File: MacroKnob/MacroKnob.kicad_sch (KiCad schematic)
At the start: 6 parts, among them SW1 RotaryEncoder_Switch_MP, U2 Sparkfun_Pro_Micro

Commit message: update schematic & pcb
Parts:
- added R4, R5, R6, R7: 10K, Resistor_THT:R_Axial_DIN0204_L3.6mm_D1.6mm_P5.08mm_Horizontal, symbol Device:R
- added SW2: Up, Button_Switch_SMD:SW_SPST_CK_RS282G05A3, symbol Switch:SW_Push
- added SW3: Down, Button_Switch_SMD:SW_SPST_CK_RS282G05A3, symbol Switch:SW_Push
- added SW4: H, Button_Switch_SMD:SW_SPST_CK_RS282G05A3, symbol Switch:SW_Push
- added SW5: *, Button_Switch_SMD:SW_SPST_CK_RS282G05A3, symbol Switch:SW_Push
- R1, R2, R3: value R -> 10K
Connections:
- net VCC 5V: now reaches R2.1
- net VCC 5V: now also R3.2
- net DT: now reaches R2.2, SW1.B
- net CLK: now reaches R3.1
- net CLK: now also SW1.A
- net GND: now reaches SW1.C, SW1.S2
- net GND: now also SW2.2, SW3.2, SW4.2, SW5.2
- net SW: now reaches R1.1
- new net: R6.1, SW4.1
- new net: R4.1, SW2.1
- new net: R5.1, SW3.1
- new net: R7.1, SW5.1
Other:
- moved on the sheet: R1, R2, R3, SW1

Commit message: update
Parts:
- added J1: Conn_01x04_Socket, Connector_Samtec:Samtec_FMC_ASP-134486-01_10x40_P1.27mm_Vertical, symbol Connector:Conn_01x04_Socket
- added R8, R9: 10K, Resistor_THT:R_Axial_DIN0204_L3.6mm_D1.6mm_P5.08mm_Horizontal, symbol Device:R
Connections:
- net GND: now also Brd1.1 (GND), J1.4 (Pin_4)
- net VCC: now reaches Brd1.2 (VCC)
- net VCC: now also J1.3 (Pin_3), R8.1, R9.1
- net at Brd1.3 (SCL): now also U2.3 (GND), J1.2 (Pin_2), R9.2
- net at Brd1.4 (SDA): now also U2.2 (D0/RX), J1.1 (Pin_1), R8.2
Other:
- moved on the sheet: Brd1

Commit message: Update Schematic
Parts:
- J1: value Conn_01x04_Socket -> I2C
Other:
- moved on the sheet: R8, R9
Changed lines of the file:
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@@
+	)
+	(junction
+		(at 63.5 86.36)
+		(diameter 0)
+		(color 0 0 0 0)
 	)
 	(junction
@@
 	)
 	(junction
-		(at 64.77 86.36)
-		(diameter 0)
-		(color 0 0 0 0)
-	)
-	(junction
 		(at 50.8 83.82)
 		(diameter 0)
@@
 	(wire
 		(pts
-			(xy 64.77 86.36) (xy 64.77 83.82)
+			(xy 63.5 86.36) (xy 63.5 83.82)
 		)
 		(stroke
@@
 	(wire
 		(pts
-			(xy 53.34 88.9) (xy 57.15 88.9)
+			(xy 53.34 88.9) (xy 55.88 88.9)
 		)
 		(stroke
@@
 	(wire
 		(pts
-			(xy 68.58 86.36) (xy 64.77 86.36)
-		)
-		(stroke
-			(width 0)
-			(type default)
-		)
-	)
-	(wire
-		(pts
 			(xy 143.51 76.2) (xy 143.51 87.63)
 		)
@@
 	(wire
 		(pts
-			(xy 64.77 86.36) (xy 64.77 88.9)
+			(xy 63.5 86.36) (xy 63.5 88.9)
 		)
 		(stroke
@@
 	(wire
 		(pts
+			(xy 63.5 86.36) (xy 68.58 86.36)
+		)
+		(stroke
+			(width 0)
+			(type default)
+		)
+	)
+	(wire
+		(pts
 			(xy 63.5 69.85) (xy 63.5 63.5)
 		)
@@
 	(wire
 		(pts
-			(xy 50.8 83.82) (xy 57.15 83.82)
+			(xy 50.8 83.82) (xy 55.88 83.82)
 		)
 		(stroke
@@
 	(symbol
 		(lib_id "Device:R")
-		(at 60.96 88.9 270)
+		(at 59.69 88.9 270)
 		(unit 1)
 		(exclude_from_sim no)
@@
 		(dnp no)
 		(property "Reference" "R9"
-			(at 60.96 88.9 90)
+			(at 59.69 88.9 90)
 			(effects
 				(font
@@
 		)
 		(property "Value" "10K"
-			(at 60.96 91.186 90)
+			(at 59.69 91.186 90)
 			(effects
 				(font
@@
 		)
 		(property "Footprint" "Resistor_THT:R_Axial_DIN0204_L3.6mm_D1.6mm_P5.08mm_Horizontal"
-			(at 60.96 87.122 90)
+			(at 59.69 87.122 90)
 			(effects
 				(font
@@
 		)
 		(property "Datasheet" "~"
-			(at 60.96 88.9 0)
+			(at 59.69 88.9 0)
 			(effects
 				(font
@@
 		)
 		(property "Description" "Resistor"
-			(at 60.96 88.9 0)
+			(at 59.69 88.9 0)
 			(effects
 				(font
@@
 			)
 		)
-		(property "Value" "Conn_01x04_Socket"
+		(property "Value" "I2C"
 			(at 92.71 74.9299 0)
 			(effects
@@
 	(symbol
 		(lib_id "Device:R")
-		(at 60.96 83.82 270)
+		(at 59.69 83.82 270)
 		(unit 1)
 		(exclude_from_sim no)
@@
 		(dnp no)
 		(property "Reference" "R8"
-			(at 60.96 83.82 90)
+			(at 59.69 83.82 90)
 			(effects
 				(font
@@
 		)
 		(property "Value" "10K"
-			(at 60.96 86.106 90)
+			(at 59.69 86.106 90)
 			(effects
 				(font
@@
 		)
 		(property "Footprint" "Resistor_THT:R_Axial_DIN0204_L3.6mm_D1.6mm_P5.08mm_Horizontal"
-			(at 60.96 82.042 90)
+			(at 59.69 82.042 90)
 			(effects
 				(font
@@
 		)
 		(property "Datasheet" "~"
-			(at 60.96 83.82 0)
+			(at 59.69 83.82 0)
 			(effects
 				(font
@@
 		)
 		(property "Description" "Resistor"
-			(at 60.96 83.82 0)
-			(effects
-				(font
+			(at 59.69 83.82 0)
+			(effects
+				(font

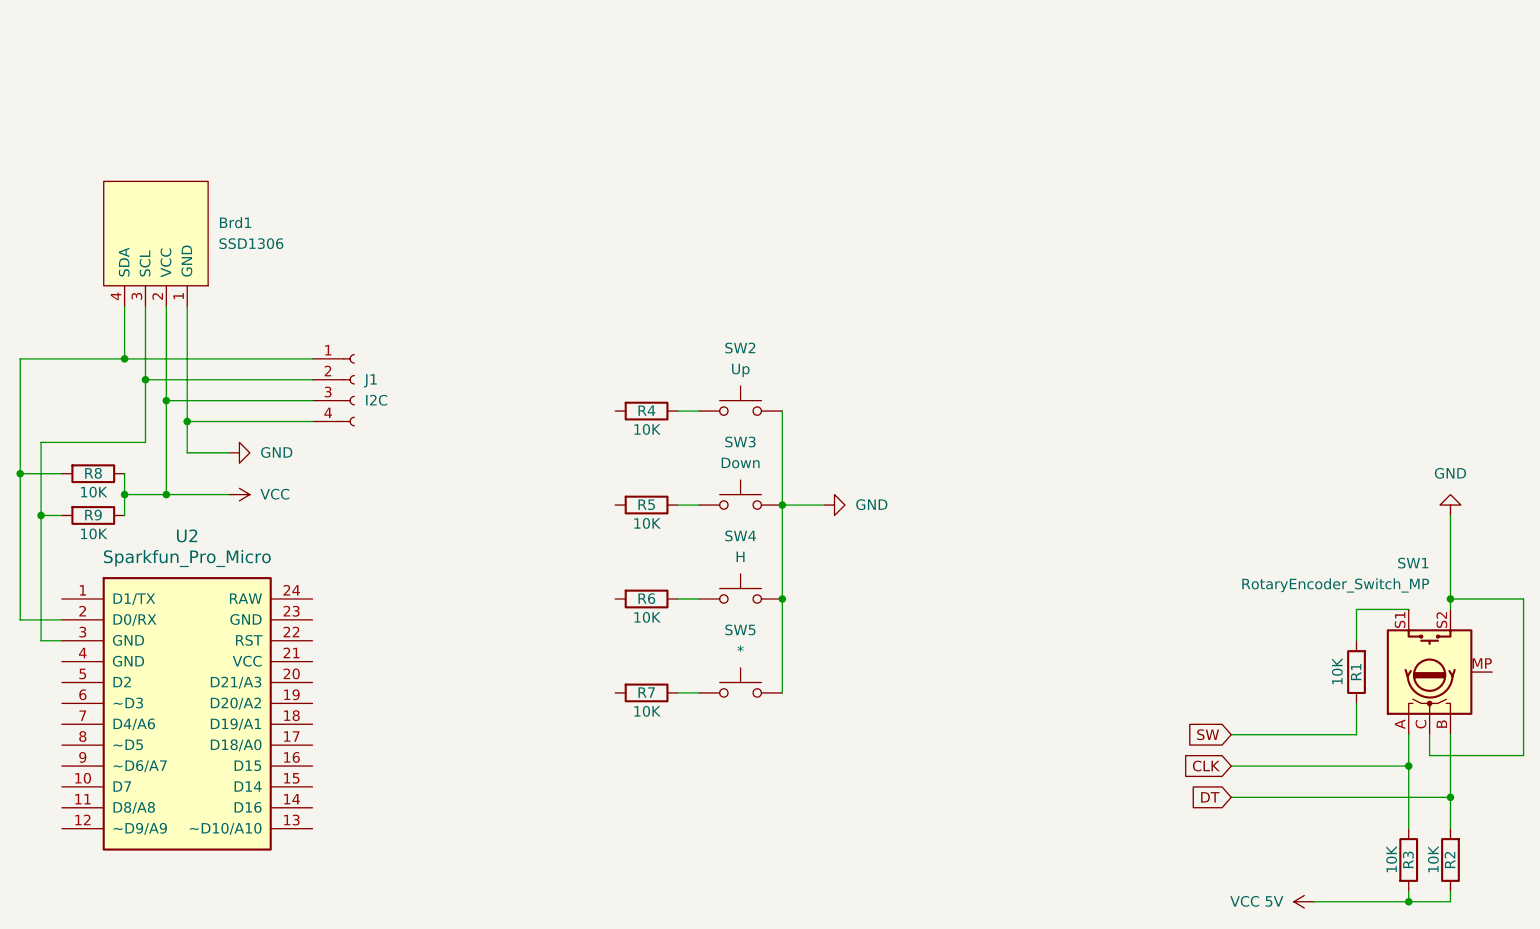
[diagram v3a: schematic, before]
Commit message: Add Script for arduino
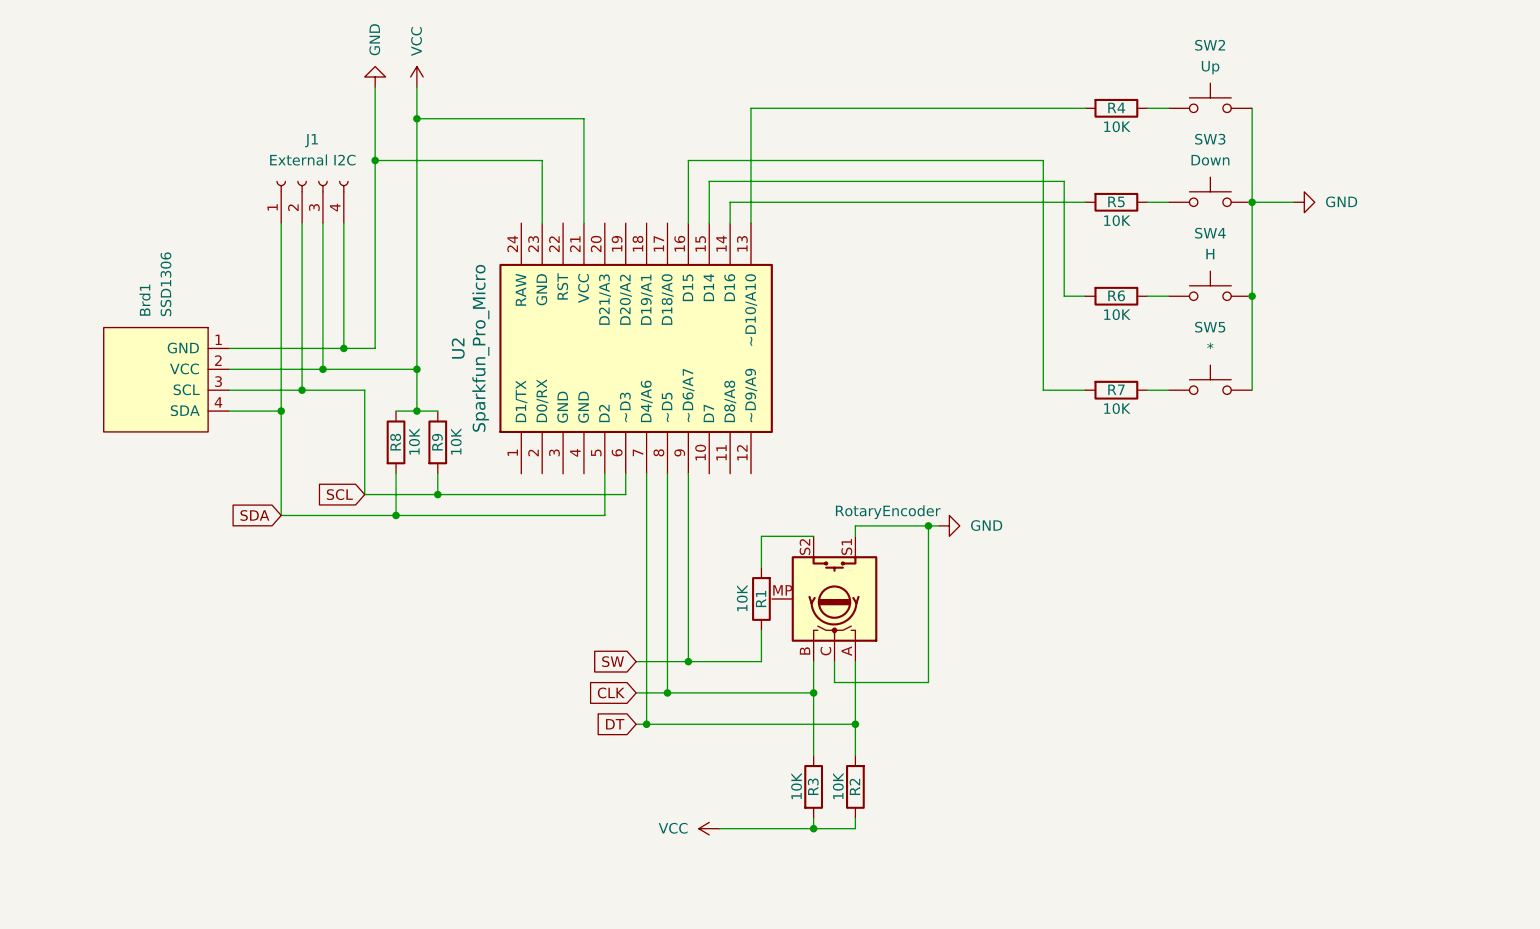
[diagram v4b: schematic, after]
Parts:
- J1: value I2C -> External I2C; footprint Connector_Samtec:Samtec_FMC_ASP-134486-01_10x40_P1.27mm_Vertical -> Connector_Hirose:Hirose_DF13-04P-1.25DSA_1x04_P1.25mm_Vertical
- SW1: value RotaryEncoder_Switch_MP -> RotaryEncoder
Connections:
- net VCC 5V is gone; now on net VCC: R2.1, R3.2
- net CLK: now also SW1.B, U2.8 (~D5); no longer SW1.A
- net DT: now also SW1.A, U2.7 (D4/A6); no longer SW1.B
- net GND: now also SW1.S1, U2.23 (GND); no longer SW1.S2
- net SW: now also U2.9 (~D6/A7)
- net VCC: now also U2.21 (VCC)
- net SCL: now reaches Brd1.3 (SCL), J1.2 (Pin_2), R9.2
- net SCL: now also U2.6 (~D3); no longer U2.3 (GND)
- net SDA: now reaches Brd1.4 (SDA), J1.1 (Pin_1), R8.2
- net SDA: now also U2.5 (D2); no longer U2.2 (D0/RX)
- net at R4.2: now also U2.13 (~D10/A10)
- net at R7.2: now also U2.16 (D15)
- net at U2.14 (D16): now also R5.2
- net at U2.15 (D14): now also R6.2
- net at R1.2: now also SW1.S2; no longer SW1.S1
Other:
- moved on the sheet: Brd1, R1, R2, R3, R4, R5, R6, R7, R8, R9, SW2, SW3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
